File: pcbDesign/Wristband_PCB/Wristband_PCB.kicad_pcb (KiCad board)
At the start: 2 copper layers, 40 x 45 mm, 5 parts, among them U1 module_adxl345, U2 SEN0344, U3 ESP32-C3_SUPERMINI_TH

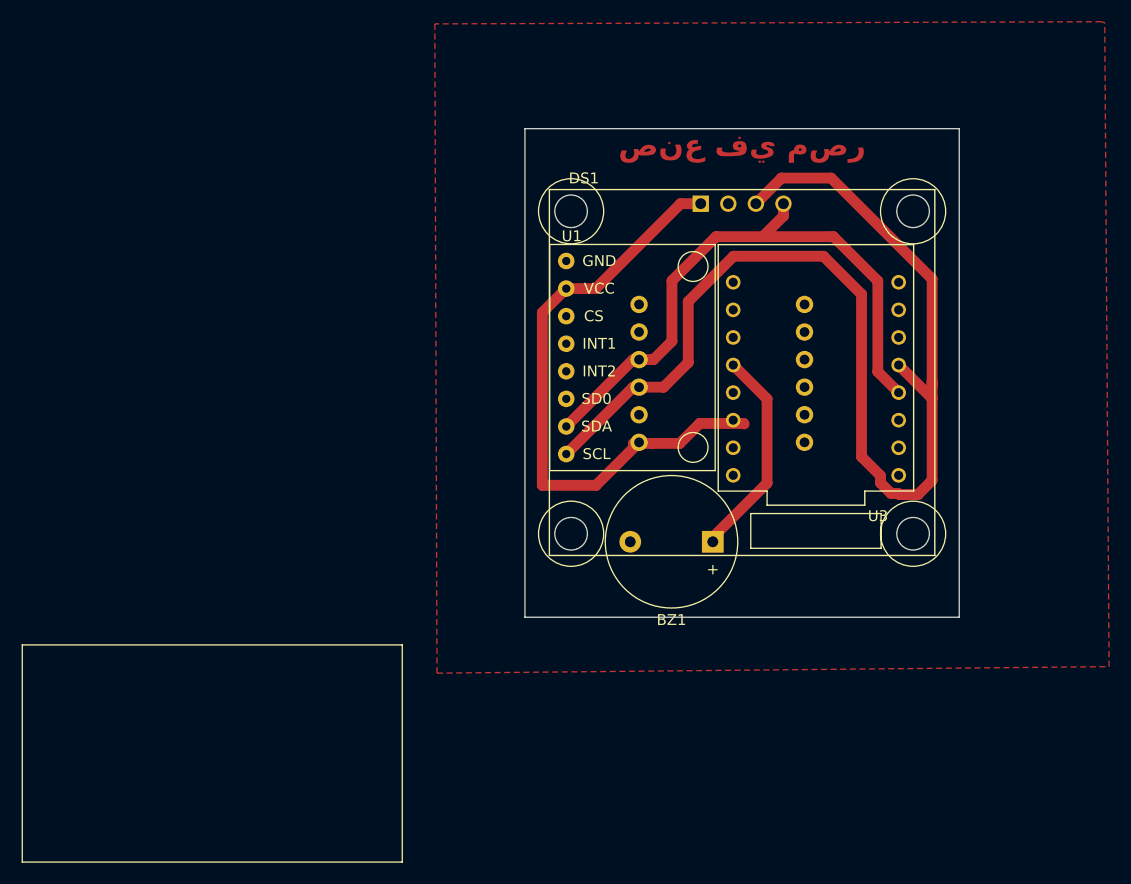
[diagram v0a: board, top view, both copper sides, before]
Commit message: added a power socket
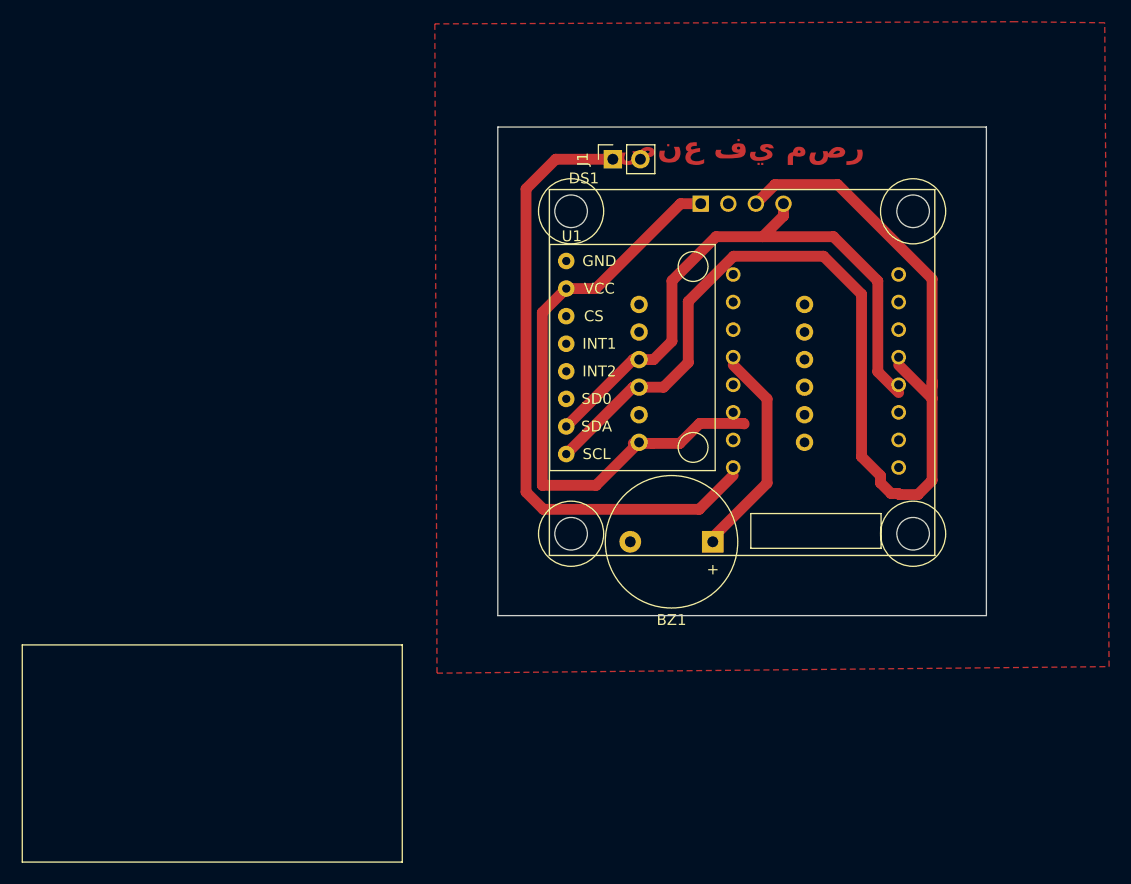
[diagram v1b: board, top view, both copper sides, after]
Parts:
- added J1: Conn_01x02_Socket, Connector_PinSocket_2.54mm:PinSocket_1x02_P2.54mm_Vertical, F.Cu at (122.6, 56.1)
- U3: moved to B.Cu
- moved U3 1.30 mm to (141.3, 76.6)
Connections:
- U3 pad 5V: unconnected-(U3-Pad5V) -> +5V
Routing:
- net +5V: track 0.00 -> 58.1 mm
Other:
- board size 40 x 45 mm -> 45 x 45 mm

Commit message: Correct_orientaion
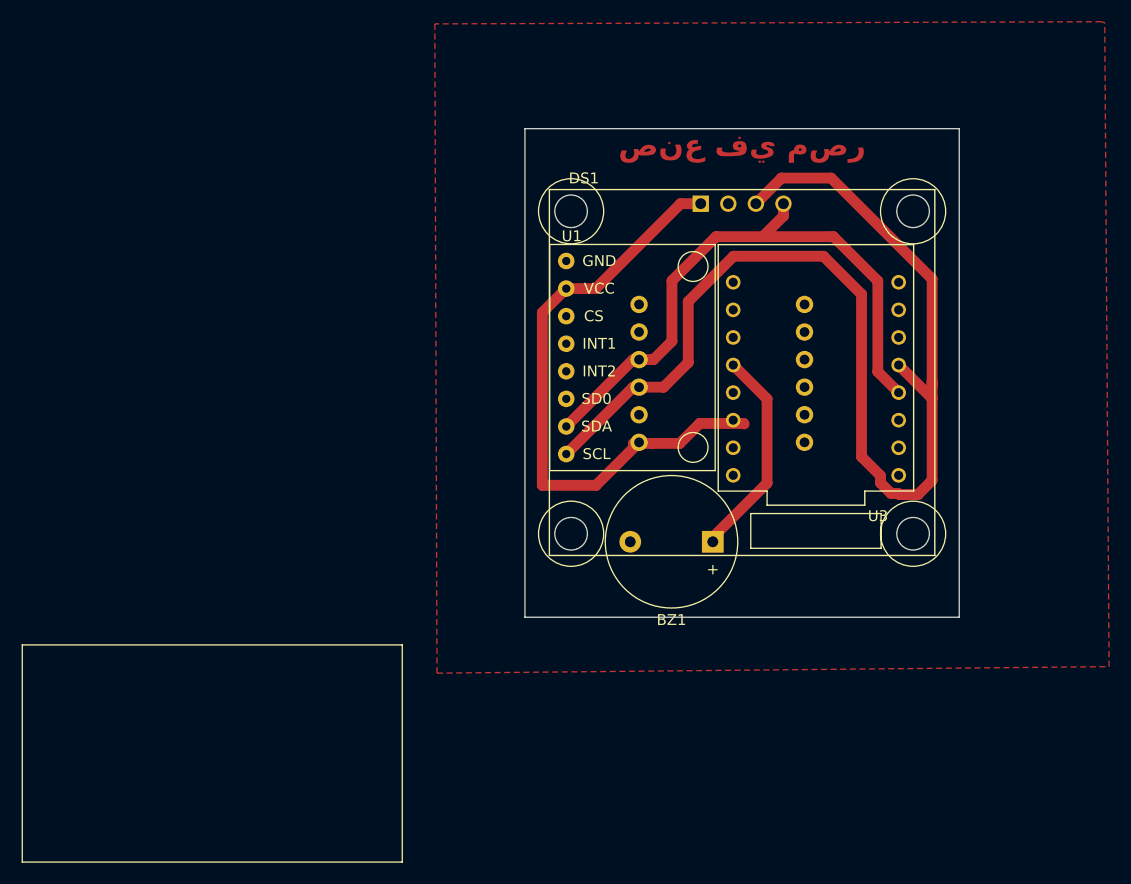
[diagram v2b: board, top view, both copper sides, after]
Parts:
- removed J1: Conn_01x02_Socket, Connector_PinSocket_2.54mm:PinSocket_1x02_P2.54mm_Vertical
- U3: moved to F.Cu
- moved U3 1.30 mm to (141.3, 75.3)
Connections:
- U3 pad 5V: +5V -> unconnected-(U3-Pad5V)
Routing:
- net +5V: track 58.1 -> 0.00 mm
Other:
- board size 45 x 45 mm -> 40 x 45 mm
